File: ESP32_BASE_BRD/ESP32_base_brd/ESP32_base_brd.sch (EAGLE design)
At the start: 22 parts, among them IC3 TPS63802DLAR, U1 ESP-WROOM-32

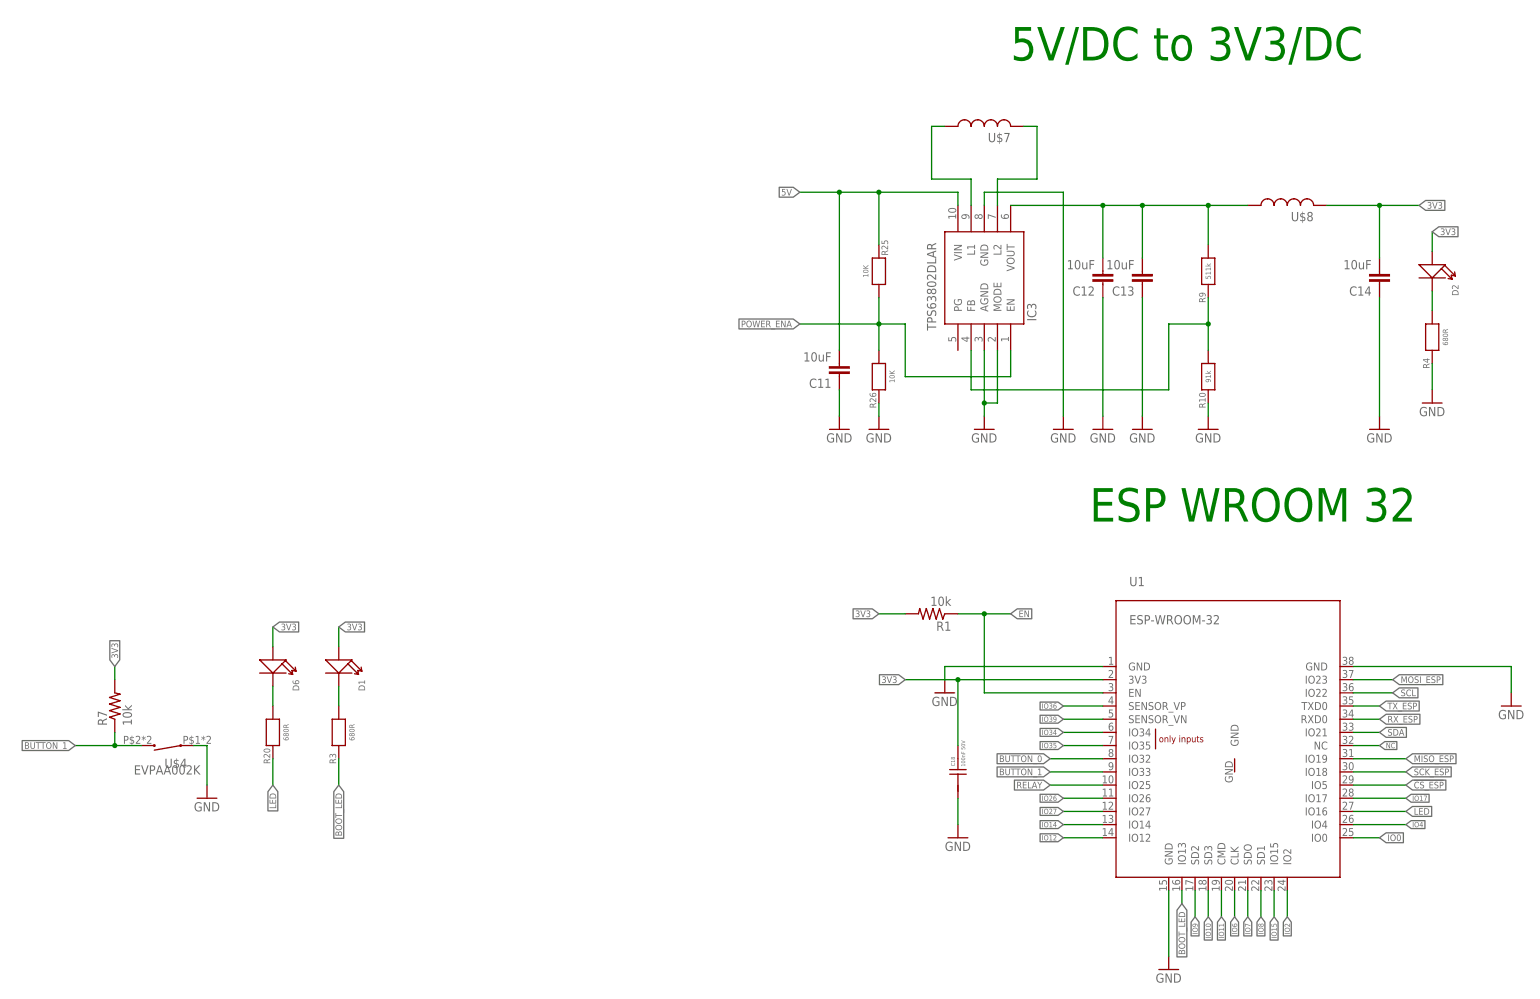
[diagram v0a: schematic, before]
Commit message: add transistor to load program without push buttons and flip boot led
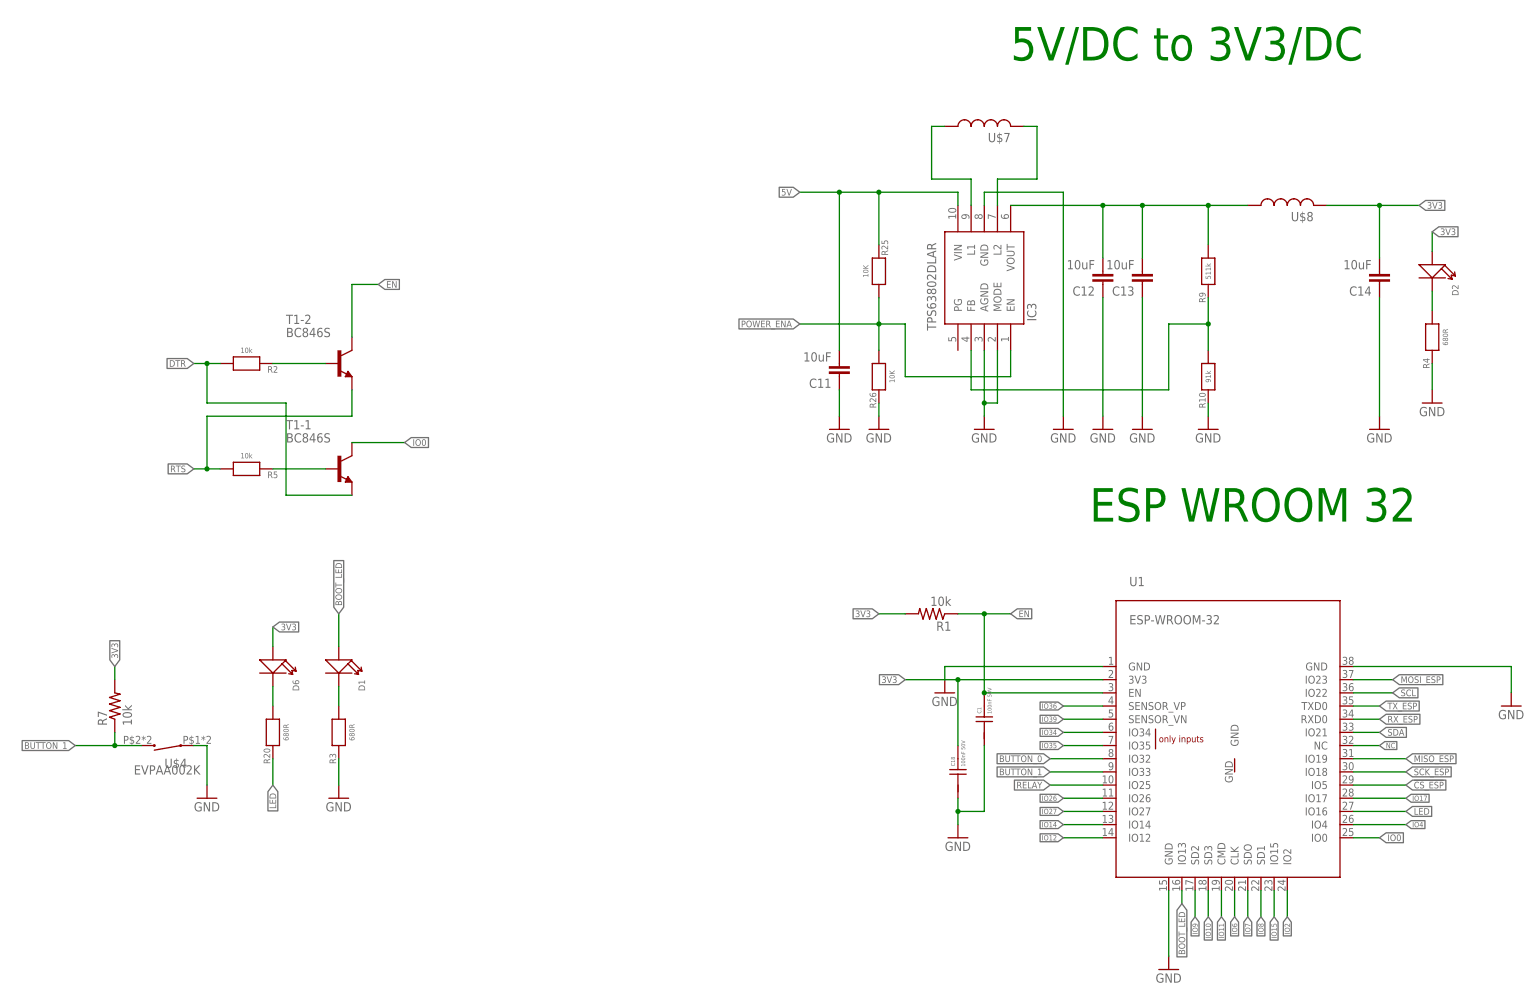
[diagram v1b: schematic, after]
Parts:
- added C1: 100nF 50V, vb_C_EC:CAPACITOR_CERAMIC_0402_100NF
- added R2, R5: 10k, vb_R_EC:RESISTOR_0402
- added T1: BC846S, BC846S:BC846S
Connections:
- new net DTR: R2.2, T1-1.E
- new net N$1: R2.1, T1-2.B
- new net N$2: R5.1, T1-1.B
- new net RTS: R5.2, T1-2.E
- net 3V3: no longer D1.+
- net BOOT_LED: now also D1.+; no longer R3.1
- net EN: now also C1.2, T1-2.C
- net GND: now also C1.1, R3.1
- net IO0: now also T1-1.C
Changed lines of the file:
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@@
 <part name="GND30" library="supply1" library_urn="urn:adsk.eagle:library:371" deviceset="GND" device=""/>
 <part name="R25" library="vb_R" deviceset="RESISTOR_0402" device="" value="10K"/>
+<part name="T1" library="BC846S" deviceset="BC846S" device=""/>
+<part name="R2" library="vb_R_EC" deviceset="RESISTOR_0402" device="" value="10k"/>
+<part name="R5" library="vb_R_EC" deviceset="RESISTOR_0402" device="" value="10k"/>
+<part name="C1" library="vb_C_EC" deviceset="CAPACITOR_CERAMIC_0402_100NF" device="" value="100nF 50V"/>
+<part name="GND1" library="SparkFun-Aesthetics" deviceset="GND" device=""/>
 </parts>
 <sheets>
@@
 <attribute name="VALUE" x="193.04" y="63.5" size="1.016" layer="96" ratio="10" rot="R270" align="center"/>
 </instance>
+<instance part="T1" gate="-1" x="91.44" y="25.4" smashed="yes">
+<attribute name="NAME" x="81.2744" y="33.02421875" size="1.77898125" layer="95"/>
+<attribute name="VALUE" x="81.2643" y="30.48786875" size="1.78075" layer="96"/>
+</instance>
+<instance part="T1" gate="-2" x="91.44" y="45.72" smashed="yes">
+<attribute name="NAME" x="81.2744" y="53.34421875" size="1.77898125" layer="95"/>
+<attribute name="VALUE" x="81.2643" y="50.80786875" size="1.78075" layer="96"/>
+</instance>
+<instance part="R2" gate="G$1" x="73.66" y="45.72" smashed="yes" rot="R180">
+<attribute name="NAME" x="79.756" y="45.212" size="1.27" layer="95" ratio="10" rot="R180"/>
+<attribute name="VALUE" x="73.66" y="48.26" size="1.016" layer="96" ratio="10" rot="R180" align="center"/>
+</instance>
+<instance part="R5" gate="G$1" x="73.66" y="25.4" smashed="yes" rot="R180">
+<attribute name="NAME" x="79.756" y="24.892" size="1.27" layer="95" ratio="10" rot="R180"/>
+<attribute name="VALUE" x="73.66" y="27.94" size="1.016" layer="96" ratio="10" rot="R180" align="center"/>
+</instance>
+<instance part="C1" gate="G$1" x="215.9" y="-22.86" smashed="yes">
+<attribute name="NAME" x="214.9475" y="-21.7805" size="0.762" layer="95" ratio="10" rot="R90" align="center-left"/>
+<attribute name="VALUE" x="216.916" y="-21.844" size="0.762" layer="96" ratio="10" rot="R90" align="center-left"/>
+</instance>
+<instance part="GND1" gate="1" x="91.44" y="-38.1" smashed="yes">
+<attribute name="VALUE" x="88.9" y="-40.64" size="1.778" layer="96"/>
+</instance>
 </instances>
 <busses>
@@
 <pinref part="GND5" gate="1" pin="GND"/>
 <pinref part="C18" gate="G$1" pin="1"/>
-<wire x1="210.82" y1="-43.18" x2="210.82" y2="-38.1" width="0.1524" layer="91"/>
+<wire x1="210.82" y1="-43.18" x2="210.82" y2="-40.64" width="0.1524" layer="91"/>
+<pinref part="C1" gate="G$1" pin="1"/>
+<wire x1="210.82" y1="-40.64" x2="210.82" y2="-38.1" width="0.1524" layer="91"/>
+<wire x1="215.9" y1="-27.94" x2="215.9" y2="-40.64" width="0.1524" layer="91"/>
+<wire x1="215.9" y1="-40.64" x2="210.82" y2="-40.64" width="0.1524" layer="91"/>
+<junction x="210.82" y="-40.64"/>
 </segment>
 <segment>
@@
 <pinref part="GND30" gate="1" pin="GND"/>
 </segment>
+<segment>
+<pinref part="GND1" gate="1" pin="GND"/>
+<pinref part="R3" gate="G$1" pin="1"/>
+<wire x1="91.44" y1="-35.56" x2="91.44" y2="-30.48" width="0.1524" layer="91"/>
+</segment>
 </net>
 <net name="!CS_ESP" class="0">
@@
 <pinref part="D6" gate="G$1" pin="+"/>
 <label x="78.74" y="-5.08" size="1.27" layer="95" xref="yes"/>
-</segment>
-<segment>
-<wire x1="91.44" y1="-5.08" x2="91.44" y2="-8.89" width="0.1524" layer="91"/>
-<pinref part="D1" gate="G$1" pin="+"/>
-<label x="91.44" y="-5.08" size="1.27" layer="95" xref="yes"/>
 </segment>
 <segment>
@@
 <wire x1="215.9" y1="-2.54" x2="220.98" y2="-2.54" width="0.1524" layer="91"/>
 <junction x="215.9" y="-2.54"/>
+<pinref part="C1" gate="G$1" pin="2"/>
+<junction x="215.9" y="-17.78"/>
+</segment>
+<segment>
+<pinref part="T1" gate="-2" pin="C"/>
+<wire x1="93.98" y1="50.8" x2="93.98" y2="60.96" width="0.1524" layer="91"/>
+<wire x1="93.98" y1="60.96" x2="99.06" y2="60.96" width="0.1524" layer="91"/>
+<label x="99.06" y="60.96" size="1.27" layer="95" xref="yes"/>
 </segment>
 </net>
@@
 </segment>
 <segment>
-<pinref part="R3" gate="G$1" pin="1"/>
-<wire x1="91.44" y1="-30.48" x2="91.44" y2="-35.56" width="0.1524" layer="91"/>
-<label x="91.44" y="-35.56" size="1.27" layer="95" rot="R270" xref="yes"/>
+<pinref part="D1" gate="G$1" pin="+"/>
+<wire x1="91.44" y1="-8.89" x2="91.44" y2="-2.54" width="0.1524" layer="91"/>
+<label x="91.44" y="-2.54" size="1.27" layer="95" rot="R90" xref="yes"/>
 </segment>
 </net>
@@
 <label x="292.1" y="-45.72" size="1.27" layer="95" xref="yes"/>
 </segment>
-</net>
+<segment>
+<pinref part="T1" gate="-1" pin="C"/>
+<wire x1="93.98" y1="30.48" x2="104.14" y2="30.48" width="0.1524" layer="91"/>
+<label x="104.14" y="30.48" size="1.27" layer="95" xref="yes"/>
+</segment>
+</net>
+<net name="N$1" class="0">
+<segment>
+<pinref part="T1" gate="-2" pin="B"/>
+<wire x1="88.9" y1="45.72" x2="78.74" y2="45.72" width="0.1524" layer="91"/>
+<pinref part="R2" gate="G$1" pin="1"/>
+</segment>
+</net>
+<net name="N$2" class="0">
+<segment>
+<pinref part="T1" gate="-1" pin="B"/>
+<wire x1="88.9" y1="25.4" x2="78.74" y2="25.4" width="0.1524" layer="91"/>
+<pinref part="R5" gate="G$1" pin="1"/>
+</segment>
+</net>
+<net name="DTR" class="0">
+<segment>
+<pinref part="R2" gate="G$1" pin="2"/>
+<wire x1="68.58" y1="45.72" x2="66.04" y2="45.72" width="0.1524" layer="91"/>
+<label x="63.5" y="45.72" size="1.27" layer="95" rot="R180" xref="yes"/>
+<pinref part="T1" gate="-1" pin="E"/>
+<wire x1="66.04" y1="45.72" x2="63.5" y2="45.72" width="0.1524" layer="91"/>
+<wire x1="93.98" y1="20.32" x2="81.28" y2="20.32" width="0.1524" layer="91"/>
+<wire x1="81.28" y1="20.32" x2="81.28" y2="38.1" width="0.1524" layer="91"/>
+<wire x1="81.28" y1="38.1" x2="66.04" y2="38.1" width="0.1524" layer="91"/>
+<wire x1="66.04" y1="38.1" x2="66.04" y2="45.72" width="0.1524" layer="91"/>
+<junction x="66.04" y="45.72"/>
+</segment>
+</net>
+<net name="RTS" class="0">
+<segment>
+<pinref part="R5" gate="G$1" pin="2"/>
+<wire x1="68.58" y1="25.4" x2="66.04" y2="25.4" width="0.1524" layer="91"/>
+<label x="63.5" y="25.4" size="1.27" layer="95" rot="R180" xref="yes"/>
+<pinref part="T1" gate="-2" pin="E"/>
+<wire x1="66.04" y1="25.4" x2="63.5" y2="25.4" width="0.1524" layer="91"/>
+<wire x1="93.98" y1="40.64" x2="93.98" y2="35.56" width="0.1524" layer="91"/>
+<wire x1="93.98" y1="35.56" x2="66.04" y2="35.56" width="0.1524" layer="91"/>
+<wire x1="66.04" y1="35.56" x2="66.04" y2="25.4" width="0.1524" layer="91"/>
+<junction x="66.04" y="25.4"/>
+</segment>
+</net>
